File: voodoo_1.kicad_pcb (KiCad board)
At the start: 2 copper layers, 69 x 43 mm, 37 parts, among them Q1 2N2222, Q2 2N2222, U1 LM308

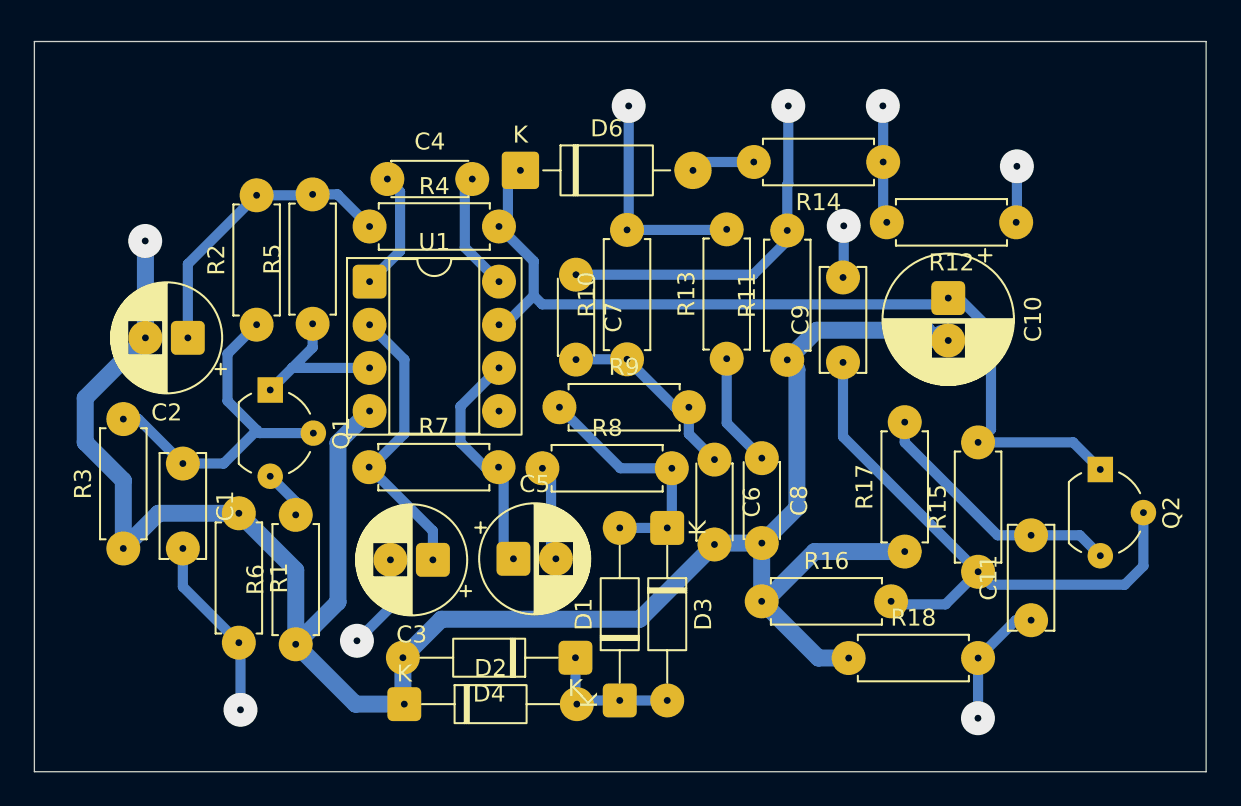
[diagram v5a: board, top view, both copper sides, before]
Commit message: ネジ穴追加、配置修整、線は0.8mm、GNDは1.0mm。
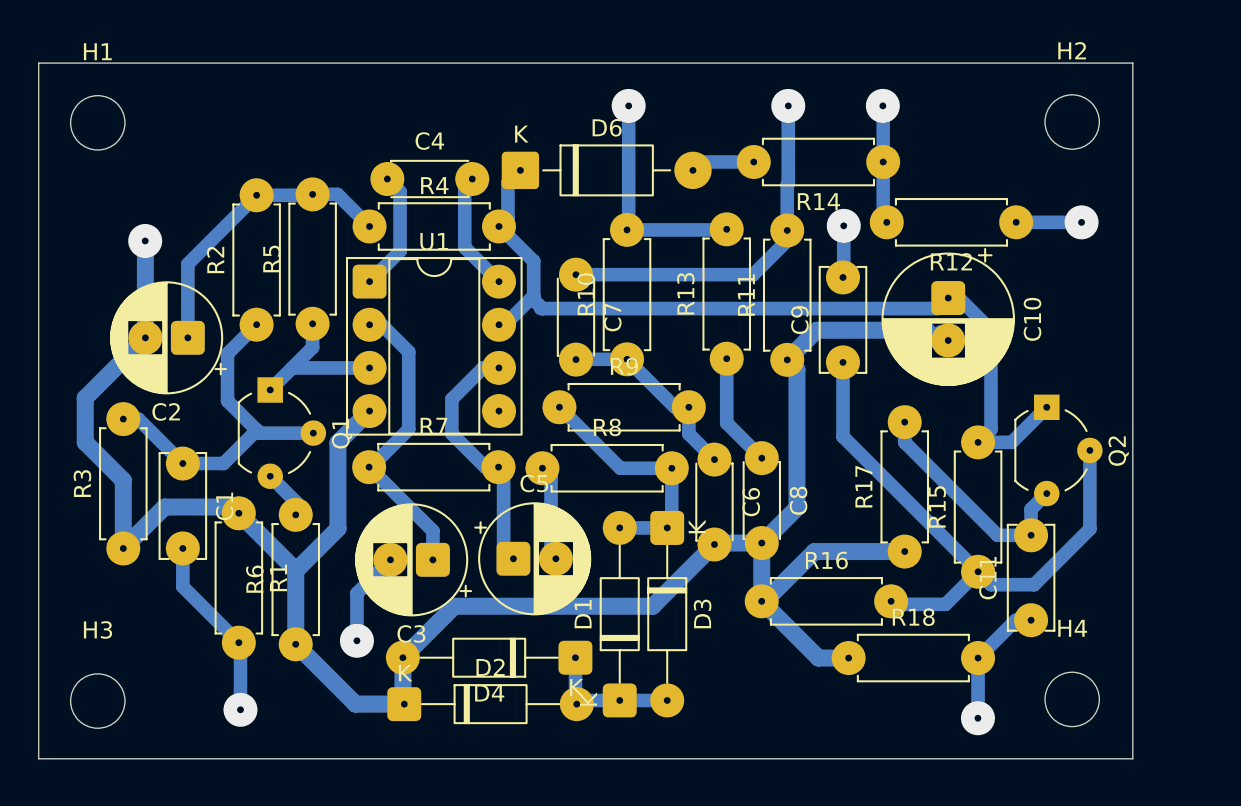
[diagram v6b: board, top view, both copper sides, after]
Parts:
- added H1: MountingHole, MountingHole:MountingHole_3.2mm_M3, F.Cu at (43.7, 80.8)
- added H2: MountingHole, MountingHole:MountingHole_3.2mm_M3, F.Cu at (101.0, 80.7)
- added H3: MountingHole, MountingHole:MountingHole_3.2mm_M3, F.Cu at (43.7, 114.8)
- added H4: MountingHole, MountingHole:MountingHole_3.2mm_M3, F.Cu at (101.0, 114.7)
- moved Q2 4.83 mm to (99.5, 97.5)
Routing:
- net GND: track 130.1 -> 126.1 mm
- net Net-(D6-K): track 54.4 -> 51.9 mm
- net Net-(Q2-E): track 15.5 -> 13.7 mm
- net Net-(C5-Pad1): track 13.9 -> 14.9 mm
- net Net-(Q2-B): track 35.2 -> 34.4 mm
- net Net-(U1--): track 17.2 -> 17.8 mm
- net Net-(SW1C-C): track 3.30 -> 3.81 mm
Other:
- board size 69 x 43 mm -> 64.4 x 41 mm
